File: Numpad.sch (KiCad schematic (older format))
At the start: 50 parts, among them J1 USB_B_Mini, SW0 MXSwitch, SW1 MXSwitch, SW2 MXSwitch, SW3 MXSwitch, SW4 MXSwitch, SW5 MXSwitch, SW6 MXSwitch, SW7 MXSwitch, SW8 MXSwitch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

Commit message: Components roughly placed in grid, connected rows and cols to processor
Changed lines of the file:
@@
 EESchema Schematic File Version 4
+LIBS:Numpad-cache
 EELAYER 30 0
 EELAYER END
@@
 Wire Wire Line
 	3150 4900 3250 4900
+Text GLabel 4750 3600 2    50   Output ~ 0
+Row1
+Text GLabel 4750 3700 2    50   Output ~ 0
+Row2
+Text GLabel 4750 3800 2    50   Output ~ 0
+Row3
+Text GLabel 4750 3900 2    50   Output ~ 0
+Row4
+Text GLabel 4750 4000 2    50   Output ~ 0
+Row5
+Text GLabel 4750 4800 2    50   Output ~ 0
+Col1
+Text GLabel 4750 4900 2    50   Output ~ 0
+Col2
+Text GLabel 4750 5000 2    50   Output ~ 0
+Col3
+Text GLabel 4750 5100 2    50   Output ~ 0
+Col4
 $EndSCHEMATC

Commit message: components roughly placed
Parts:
- removed Y1: 16MHz, Crystal:Crystal_SMD_5032-2Pin_5.0x3.2mm_HandSoldering, symbol Device:Crystal_Small
- added H1, H2, H3, H4: MountingHole, MountingHole:MountingHole_3mm_Pad, symbol Mechanical:MountingHole
- added Y1: 16MHz, Crystal:Crystal_SMD_3225-4Pin_3.2x2.5mm_HandSoldering, symbol Device:Crystal_GND24_Small
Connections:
- net labels added: D+, D-
- wire segments 82 -> 89
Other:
- moved on the sheet: C2, C3, C4, J1, R2, R3, R4, U1

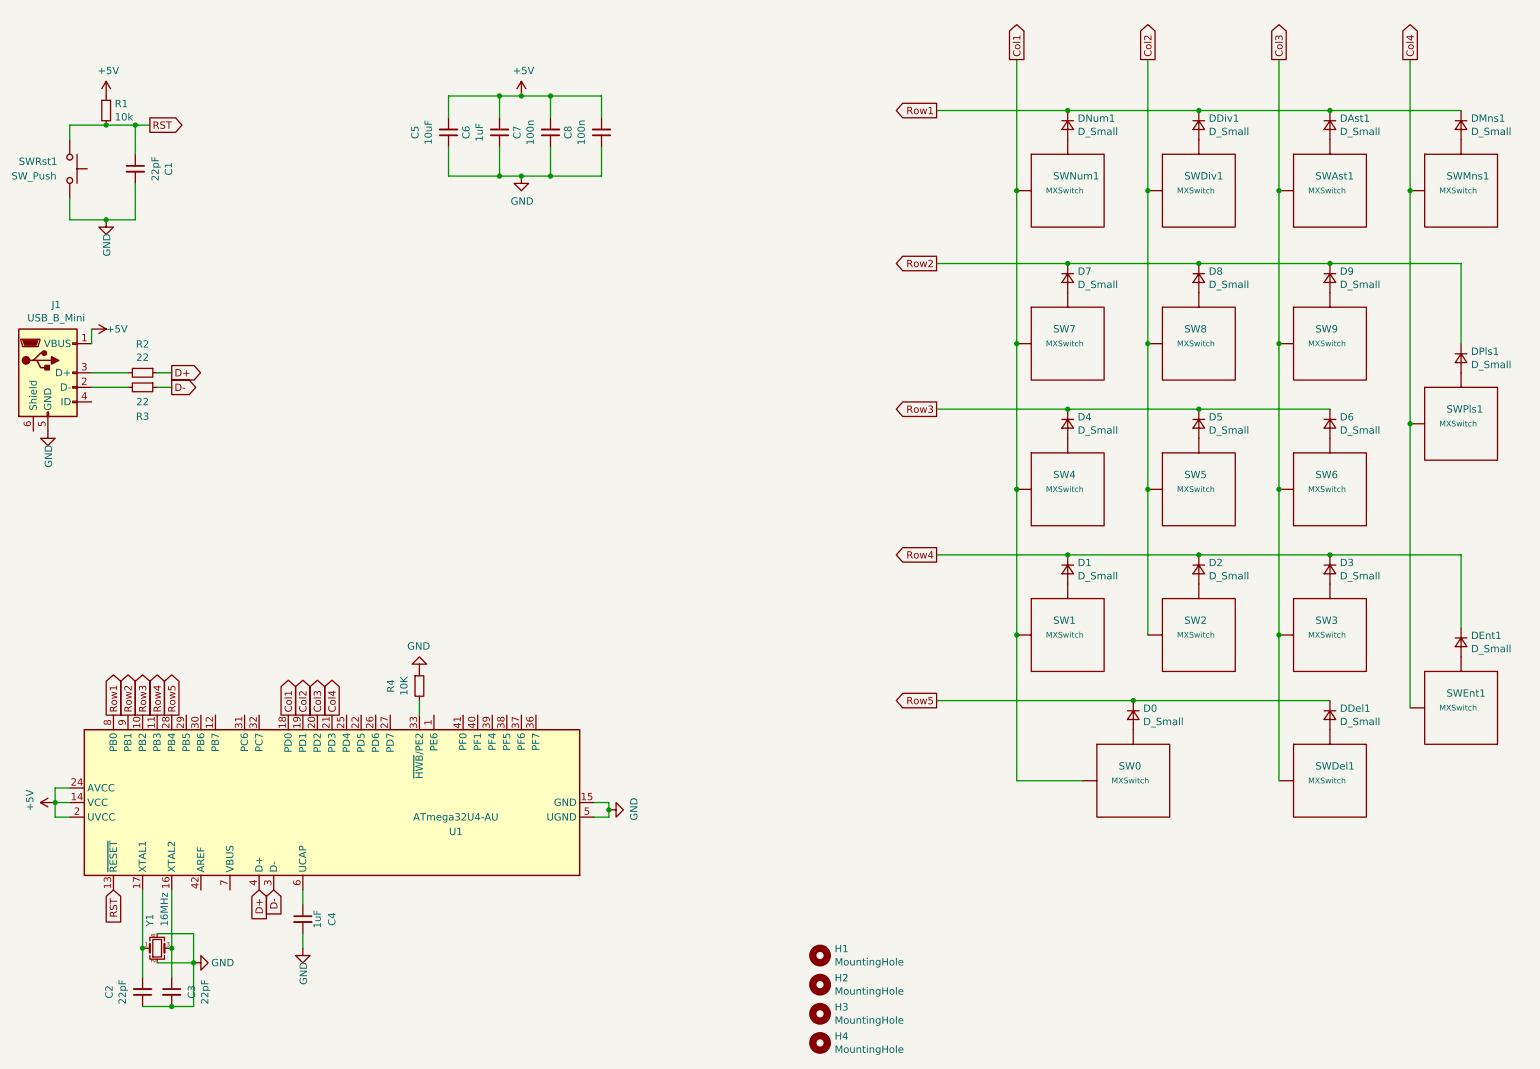
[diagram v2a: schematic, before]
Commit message: ignore bak files, went bak to standard pcb orientation
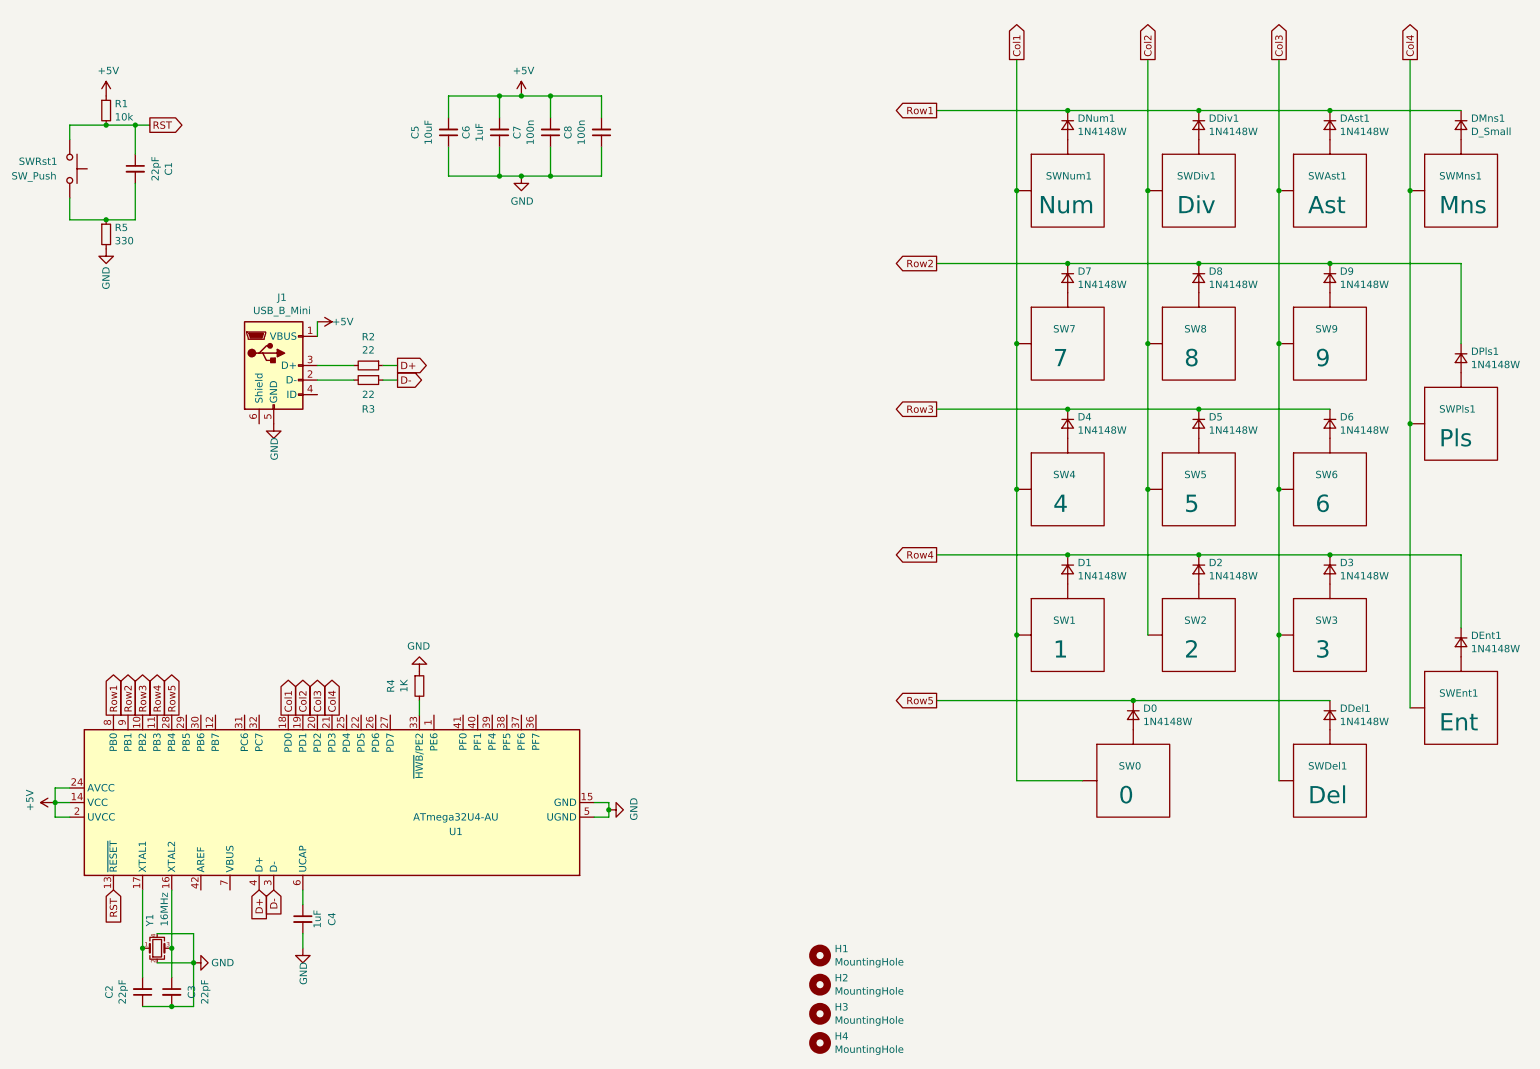
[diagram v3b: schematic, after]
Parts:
- added R5: 330, Resistor_SMD:R_1206_3216Metric_Pad1.42x1.75mm_HandSolder, symbol Device:R_Small
- D0, D1, D2, D3, D4, D5, D6, D7, D8, D9, DAst1, DDel1, DDiv1, DEnt1, DNum1, DPls1: value D_Small -> 1N4148W
- R4: value 10K -> 1K
- SW0: value MXSwitch -> 0
- SW1: value MXSwitch -> 1
- SW2: value MXSwitch -> 2
- SW3: value MXSwitch -> 3
- SW4: value MXSwitch -> 4
- SW5: value MXSwitch -> 5
- SW6: value MXSwitch -> 6
- SW7: value MXSwitch -> 7
- SW8: value MXSwitch -> 8
- SW9: value MXSwitch -> 9
- SWAst1: value MXSwitch -> Ast
- SWDel1: value MXSwitch -> Del
- SWDiv1: value MXSwitch -> Div
- SWEnt1: value MXSwitch -> Ent
- SWMns1: value MXSwitch -> Mns
- SWNum1: value MXSwitch -> Num
- SWPls1: value MXSwitch -> Pls
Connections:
- net GND: now also R5.2; no longer C1.2, SWRst1.2
- new net: C1.2, R5.1, SWRst1.2
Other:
- moved on the sheet: J1, R2, R3

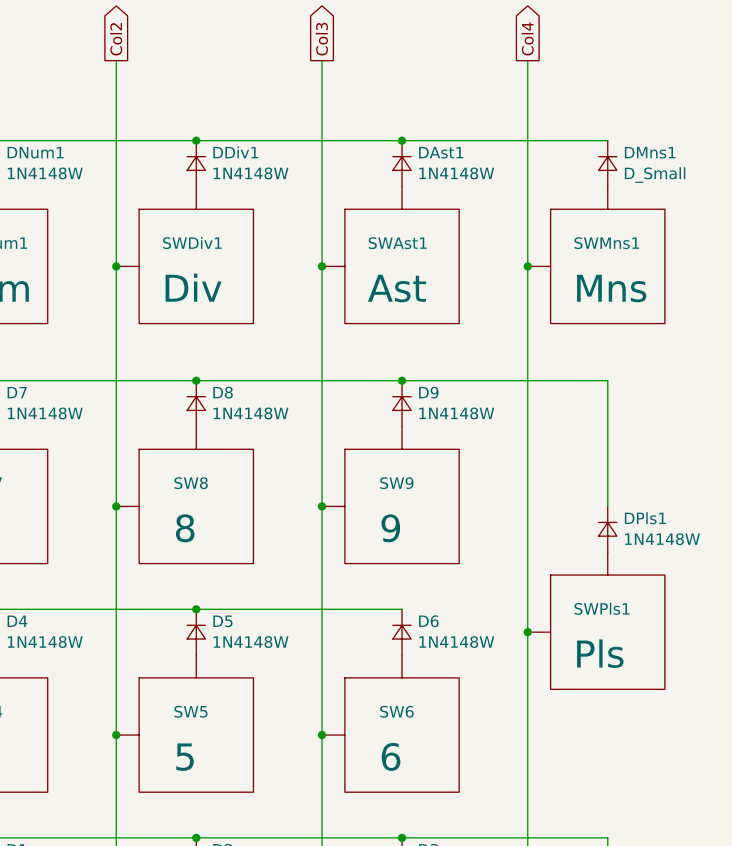
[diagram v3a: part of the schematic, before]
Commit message: MX labels updated, missed diode spec
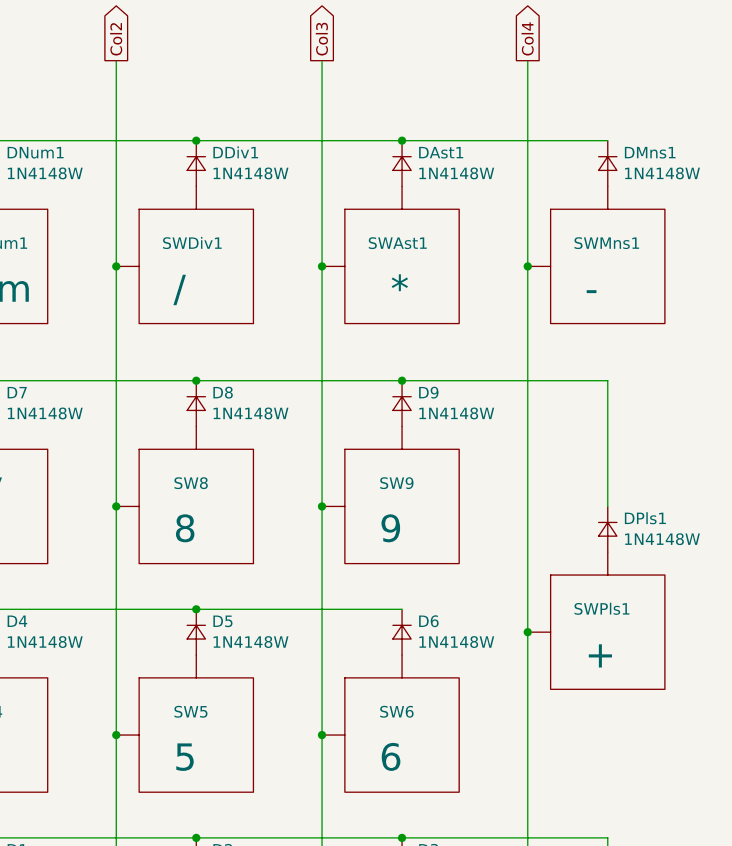
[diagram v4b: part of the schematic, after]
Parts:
- DMns1: value D_Small -> 1N4148W
- SWAst1: value Ast -> *
- SWDiv1: value Div -> /
- SWMns1: value Mns -> -
- SWPls1: value Pls -> +
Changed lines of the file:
@@
 P 8750 1700
 F 0 "SWDiv1" H 8600 1800 50  0000 L CNN
-F 1 "Div" H 8600 1600 118 0000 L CNN
+F 1 "/" H 8650 1600 118 0000 L CNN
 F 2 "AcheronMX:MX100" H 8750 1700 50  0001 C CNN
 F 3 "" H 8750 1700 50  0001 C CNN
@@
 P 9650 1700
 F 0 "SWAst1" H 9500 1800 50  0000 L CNN
-F 1 "Ast" H 9500 1600 118 0000 L CNN
+F 1 "*" H 9600 1600 118 0000 L CNN
 F 2 "AcheronMX:MX100" H 9650 1700 50  0001 C CNN
 F 3 "" H 9650 1700 50  0001 C CNN
@@
 P 10550 1700
 F 0 "SWMns1" H 10400 1800 50  0000 L CNN
-F 1 "Mns" H 10400 1600 118 0000 L CNN
+F 1 "-" H 10450 1600 118 0000 L CNN
 F 2 "AcheronMX:MX100" H 10550 1700 50  0001 C CNN
 F 3 "" H 10550 1700 50  0001 C CNN
@@
 P 10550 3300
 F 0 "SWPls1" H 10400 3400 50  0000 L CNN
-F 1 "Pls" H 10400 3200 118 0000 L CNN
+F 1 "+" H 10450 3200 118 0000 L CNN
 F 2 "AcheronMX:MX200V" H 10550 3300 50  0001 C CNN
 F 3 "" H 10550 3300 50  0001 C CNN
@@
 P 10550 1250
 F 0 "DMns1" V 10504 1318 50  0000 L CNN
-F 1 "D_Small" V 10595 1318 50  0000 L CNN
+F 1 "1N4148W" V 10595 1318 50  0000 L CNN
 F 2 "Diode_SMD:D_SOD-123" V 10550 1250 50  0001 C CNN
 F 3 "~" V 10550 1250 50  0001 C CNN

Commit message: rotated stabiliser holes for tighter pcb
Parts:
- SW0: footprint AcheronMX:MX200 -> AcheronMX:MX200R
- SWEnt1, SWPls1: footprint AcheronMX:MX200V -> AcheronMX:MX200VR
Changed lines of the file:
@@
 F 0 "SWPls1" H 10400 3400 50  0000 L CNN
 F 1 "+" H 10450 3200 118 0000 L CNN
-F 2 "AcheronMX:MX200V" H 10550 3300 50  0001 C CNN
+F 2 "AcheronMX:MX200VR" H 10550 3300 50  0001 C CNN
 F 3 "" H 10550 3300 50  0001 C CNN
 	1    10550 3300
@@
 F 0 "SWEnt1" H 10400 5350 50  0000 L CNN
 F 1 "Ent" H 10400 5150 118 0000 L CNN
-F 2 "AcheronMX:MX200V" H 10550 5250 50  0001 C CNN
+F 2 "AcheronMX:MX200VR" H 10550 5250 50  0001 C CNN
 F 3 "" H 10550 5250 50  0001 C CNN
 	1    10550 5250
@@
 F 0 "SW0" H 8200 5850 50  0000 L CNN
 F 1 "0" H 8200 5650 118 0000 L CNN
-F 2 "AcheronMX:MX200" H 8300 5750 50  0001 C CNN
+F 2 "AcheronMX:MX200R" H 8300 5750 50  0001 C CNN
 F 3 "" H 8300 5750 50  0001 C CNN
 	1    8300 5750

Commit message: copied aio3's capacitor settings and fuse placement
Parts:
- added F1: 500mA, Fuse:Fuse_1206_3216Metric_Pad1.42x1.75mm_HandSolder, symbol Device:Polyfuse_Small
- C6: value 1uF -> 0.1uF
- C7: value 100n -> 0.1uF
- C8: value 100n -> 01.uF
- R4: value 1K -> 10k
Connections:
- net +5V: now also F1.1; no longer J1.1 (VBUS)
- new net VCC: F1.2, J1.1 (VBUS)
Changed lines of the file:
@@
 P 3950 1300
 F 0 "C6" V 4179 1300 50  0000 C CNN
-F 1 "1uF" V 4088 1300 50  0000 C CNN
+F 1 "0.1uF" V 4088 1300 50  0000 C CNN
 F 2 "Capacitor_SMD:C_0805_2012Metric_Pad1.15x1.40mm_HandSolder" H 3950 1300 50  0001 C CNN
 F 3 "~" H 3950 1300 50  0001 C CNN
@@
 P 4650 1300
 F 0 "C8" V 4879 1300 50  0000 C CNN
-F 1 "100n" V 4788 1300 50  0000 C CNN
+F 1 "01.uF" V 4788 1300 50  0000 C CNN
 F 2 "Capacitor_SMD:C_0805_2012Metric_Pad1.15x1.40mm_HandSolder" H 4650 1300 50  0001 C CNN
 F 3 "~" H 4650 1300 50  0001 C CNN
@@
 P 4300 1300
 F 0 "C7" V 4529 1300 50  0000 C CNN
-F 1 "100n" V 4438 1300 50  0000 C CNN
+F 1 "0.1uF" V 4438 1300 50  0000 C CNN
 F 2 "Capacitor_SMD:C_0805_2012Metric_Pad1.15x1.40mm_HandSolder" H 4300 1300 50  0001 C CNN
 F 3 "~" H 4300 1300 50  0001 C CNN
@@
 P 3400 5100
 F 0 "R4" V 3204 5100 50  0000 C CNN
-F 1 "1K" V 3295 5100 50  0000 C CNN
+F 1 "10k" V 3295 5100 50  0000 C CNN
 F 2 "Resistor_SMD:R_1206_3216Metric_Pad1.42x1.75mm_HandSolder" H 3400 5100 50  0001 C CNN
 F 3 "~" H 3400 5100 50  0001 C CNN
@@
 L power:+5V #PWR04
 U 1 1 5D778839
-P 2700 2600
-F 0 "#PWR04" H 2700 2450 50  0001 C CNN
-F 1 "+5V" V 2700 2700 50  0000 L CNN
-F 2 "" H 2700 2600 50  0001 C CNN
-F 3 "" H 2700 2600 50  0001 C CNN
-	1    2700 2600
+P 3550 2500
+F 0 "#PWR04" H 3550 2350 50  0001 C CNN
+F 1 "+5V" V 3550 2600 50  0000 L CNN
+F 2 "" H 3550 2500 50  0001 C CNN
+F 3 "" H 3550 2500 50  0001 C CNN
+	1    3550 2500
 	0    1    1    0
 $EndComp
@@
 Text GLabel 2400 6500 3    50   Input ~ 0
 D-
-Wire Wire Line
-	2700 2600 2700 2700
 $Comp
 L Device:Crystal_GND24_Small Y1
@@
 	0    1    1    0
 $EndComp
+$Comp
+L Device:Polyfuse_Small F1
+U 1 1 5D84253D
+P 3250 2500
+F 0 "F1" V 3045 2500 50  0000 C CNN
+F 1 "500mA" V 3136 2500 50  0000 C CNN
+F 2 "Fuse:Fuse_1206_3216Metric_Pad1.42x1.75mm_HandSolder" H 3300 2300 50  0001 L CNN
+F 3 "~" H 3250 2500 50  0001 C CNN
+	1    3250 2500
+	0    1    1    0
+$EndComp
+$Comp
+L power:VCC #PWR0101
+U 1 1 5D846B17
+P 2850 2500
+F 0 "#PWR0101" H 2850 2350 50  0001 C CNN
+F 1 "VCC" H 2867 2673 50  0000 C CNN
+F 2 "" H 2850 2500 50  0001 C CNN
+F 3 "" H 2850 2500 50  0001 C CNN
+	1    2850 2500
+	1    0    0    -1
+$EndComp
+Wire Wire Line
+	2700 2700 2850 2700
+Wire Wire Line
+	2850 2700 2850 2500
+Wire Wire Line
+	2850 2500 3150 2500
+Connection ~ 2850 2500
+Wire Wire Line
+	3350 2500 3550 2500
 $EndSCHEMATC
